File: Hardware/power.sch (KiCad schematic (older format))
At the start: 21 parts, among them IC201 FT232RQ, P201 USB_OTG, P202 CONN_01X02, U201 MCP1700T-3302E/TT

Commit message: initial footprint assignments
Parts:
- C201: renamed from C205; footprint (none) -> Capacitors_SMD:C_0805
- C202: renamed from C201; footprint (none) -> Capacitors_SMD:C_1206
- C203: renamed from C202; footprint (none) -> Capacitors_SMD:C_0805
- C204: renamed from C206; footprint (none) -> Capacitors_SMD:C_0805
- C205: renamed from C203; footprint (none) -> Capacitors_SMD:C_0805
- C206: renamed from C204; footprint (none) -> Capacitors_SMD:C_0805
- D201, D202: footprint (none) -> Diodes_SMD:D_0805
- D203, D204: footprint (none) -> LEDs:LED_0805
- IC201: footprint QFN-32 -> Housings_DFN_QFN:QFN-32-1EP_5x5mm_Pitch0.5mm
- P202: footprint (none) -> Pin_Headers:Pin_Header_Straight_1x02
- R201, R202, R203, R204, R205, R206: footprint (none) -> Resistors_SMD:R_0805
- U201: footprint (none) -> TO_SOT_Packages_SMD:SOT-23
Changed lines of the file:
@@
 F 0 "U201" H 6955 1380 50  0000 C CNN
 F 1 "MCP1700T-3302E/TT" H 6855 1880 50  0000 C CNN
-F 2 "" H 6855 1680 50  0000 C CNN
+F 2 "TO_SOT_Packages_SMD:SOT-23" H 6855 1680 50  0001 C CNN
 F 3 "http://ww1.microchip.com/downloads/en/DeviceDoc/20001826C.pdf" H 6855 1680 50  0001 C CNN
 F 4 "Value" H 6855 1580 60  0001 C CNN "Fieldname"
@@
 F 0 "IC201" H 5790 5865 50  0000 C CNN
 F 1 "FT232RQ" H 6790 3905 50  0000 C CNN
-F 2 "QFN-32" H 6340 4615 50  0000 C CIN
+F 2 "Housings_DFN_QFN:QFN-32-1EP_5x5mm_Pitch0.5mm" H 6340 4615 50  0000 C CIN
 F 3 "http://www.ftdichip.com/Support/Documents/DataSheets/ICs/DS_FT232R.pdf" H 6340 4615 50  0001 C CNN
 F 4 "Value" H 6340 4615 60  0001 C CNN "Fieldname"
@@
 Regulator Power Filtering Requirements:  1uF on input and output
 $Comp
-L C_Small C202
+L C_Small C203
 U 1 1 58D7EC21
 P 5165 3675
-F 0 "C202" H 5175 3745 50  0000 L CNN
+F 0 "C203" H 5175 3745 50  0000 L CNN
 F 1 "0.1u" H 5175 3595 50  0000 L CNN
-F 2 "" H 5165 3675 50  0000 C CNN
+F 2 "Capacitors_SMD:C_0805" H 5165 3675 50  0001 C CNN
 F 3 "" H 5165 3675 50  0000 C CNN
 F 4 "Value" H 5165 3675 60  0001 C CNN "Fieldname"
@@
 $EndComp
 $Comp
-L C_Small C201
+L C_Small C202
 U 1 1 58D7EC71
 P 4950 3675
-F 0 "C201" H 4960 3745 50  0000 L CNN
+F 0 "C202" H 4960 3745 50  0000 L CNN
 F 1 "4.7u" H 4960 3595 50  0000 L CNN
-F 2 "" H 4950 3675 50  0000 C CNN
+F 2 "Capacitors_SMD:C_1206" H 4950 3675 50  0001 C CNN
 F 3 "" H 4950 3675 50  0000 C CNN
 F 4 "Value" H 4950 3675 60  0001 C CNN "Fieldname"
@@
 $EndComp
 $Comp
-L GND #PWR204
+L GND #PWR010
 U 1 1 58D7ECC1
 P 5075 3870
-F 0 "#PWR204" H 5075 3620 50  0001 C CNN
+F 0 "#PWR010" H 5075 3620 50  0001 C CNN
 F 1 "GND" H 5075 3720 50  0000 C CNN
 F 2 "" H 5075 3870 50  0000 C CNN
@@
 $EndComp
 $Comp
-L C_Small C203
+L C_Small C205
 U 1 1 58D7EDD8
 P 6360 1580
-F 0 "C203" H 6370 1650 50  0000 L CNN
+F 0 "C205" H 6370 1650 50  0000 L CNN
 F 1 "0.1u" H 6370 1500 50  0000 L CNN
-F 2 "" H 6360 1580 50  0000 C CNN
+F 2 "Capacitors_SMD:C_0805" H 6360 1580 50  0001 C CNN
 F 3 "" H 6360 1580 50  0000 C CNN
 F 4 "Value" H 6360 1580 60  0001 C CNN "Fieldname"
@@
 $EndComp
 $Comp
-L GND #PWR207
+L GND #PWR011
 U 1 1 58D7EF23
 P 6360 1750
-F 0 "#PWR207" H 6360 1500 50  0001 C CNN
+F 0 "#PWR011" H 6360 1500 50  0001 C CNN
 F 1 "GND" H 6360 1600 50  0000 C CNN
 F 2 "" H 6360 1750 50  0000 C CNN
@@
 FTDI 3V3 Pin needs 0.1uF cap
 $Comp
-L C_Small C204
+L C_Small C206
 U 1 1 58D7F457
 P 7310 1580
-F 0 "C204" H 7320 1650 50  0000 L CNN
+F 0 "C206" H 7320 1650 50  0000 L CNN
 F 1 "0.1u" H 7320 1500 50  0000 L CNN
-F 2 "" H 7310 1580 50  0000 C CNN
+F 2 "Capacitors_SMD:C_0805" H 7310 1580 50  0001 C CNN
 F 3 "" H 7310 1580 50  0000 C CNN
 F 4 "Value" H 7310 1580 60  0001 C CNN "Fieldname"
@@
 $EndComp
 $Comp
-L GND #PWR209
+L GND #PWR012
 U 1 1 58D7F45E
 P 7310 1750
-F 0 "#PWR209" H 7310 1500 50  0001 C CNN
+F 0 "#PWR012" H 7310 1500 50  0001 C CNN
 F 1 "GND" H 7310 1600 50  0000 C CNN
 F 2 "" H 7310 1750 50  0000 C CNN
@@
 $EndComp
 $Comp
-L GND #PWR208
+L GND #PWR013
 U 1 1 58D7F4D0
 P 6855 1835
-F 0 "#PWR208" H 6855 1585 50  0001 C CNN
+F 0 "#PWR013" H 6855 1585 50  0001 C CNN
 F 1 "GND" H 6855 1685 50  0000 C CNN
 F 2 "" H 6855 1835 50  0000 C CNN
@@
 F 0 "L201" H 4710 3575 50  0000 L CNN
 F 1 "40nH" H 4710 3475 50  0000 L CNN
-F 2 "" V 4565 3525 50  0000 C CNN
+F 2 "" V 4565 3525 50  0001 C CNN
 F 3 "http://media.digikey.com/pdf/Data%20Sheets/Steward%20PDFs/Part%20Number%20Guide.pdf" H 4635 3525 50  0001 C CNN
 F 4 "Value" H 4635 3525 60  0001 C CNN "Fieldname"
@@
 $EndComp
 $Comp
-L C_Small C205
+L C_Small C201
 U 1 1 58D87D1A
 P 4345 3625
-F 0 "C205" H 4355 3695 50  0000 L CNN
+F 0 "C201" H 4355 3695 50  0000 L CNN
 F 1 "10nF" H 4355 3545 50  0000 L CNN
-F 2 "" H 4345 3625 50  0000 C CNN
+F 2 "Capacitors_SMD:C_0805" H 4345 3625 50  0001 C CNN
 F 3 "" H 4345 3625 50  0000 C CNN
 F 4 "Value" H 4345 3625 60  0001 C CNN "Fieldname"
@@
 $EndComp
 $Comp
-L GND #PWR202
+L GND #PWR014
 U 1 1 58D87E55
 P 4345 3790
-F 0 "#PWR202" H 4345 3540 50  0001 C CNN
+F 0 "#PWR014" H 4345 3540 50  0001 C CNN
 F 1 "GND" H 4345 3640 50  0000 C CNN
 F 2 "" H 4345 3790 50  0000 C CNN
@@
 F 0 "P201" H 3790 4195 50  0000 C CNN
 F 1 "USB_OTG" H 3465 4520 50  0000 C CNN
-F 2 "" V 3415 4220 50  0000 C CNN
+F 2 "" V 3415 4220 50  0001 C CNN
 F 3 "" V 3415 4220 50  0000 C CNN
 	1    3465 4320
@@
 $EndComp
 $Comp
-L GND #PWR201
+L GND #PWR015
 U 1 1 58DED01C
 P 3765 4850
-F 0 "#PWR201" H 3765 4600 50  0001 C CNN
+F 0 "#PWR015" H 3765 4600 50  0001 C CNN
 F 1 "GND" H 3765 4700 50  0000 C CNN
 F 2 "" H 3765 4850 50  0000 C CNN
@@
 F 0 "P202" H 4640 1680 50  0000 C CNN
 F 1 "CONN_01X02" V 4740 1530 50  0000 C CNN
-F 2 "" H 4640 1530 50  0000 C CNN
+F 2 "Pin_Headers:Pin_Header_Straight_1x02" H 4640 1530 50  0001 C CNN
 F 3 "" H 4640 1530 50  0000 C CNN
 	1    4640 1530
@@
 $EndComp
 $Comp
-L GND #PWR203
+L GND #PWR016
 U 1 1 58DEDB6A
 P 4840 1720
-F 0 "#PWR203" H 4840 1470 50  0001 C CNN
+F 0 "#PWR016" H 4840 1470 50  0001 C CNN
 F 1 "GND" H 4840 1570 50  0000 C CNN
 F 2 "" H 4840 1720 50  0000 C CNN
@@
 F 0 "D201" H 5015 1560 50  0000 L CNN
 F 1 "D_Schottky_Small" H 4785 1400 50  0000 L CNN
-F 2 "" V 5065 1480 50  0000 C CNN
+F 2 "Diodes_SMD:D_0805" V 5065 1480 50  0001 C CNN
 F 3 "" V 5065 1480 50  0000 C CNN
 	1    5065 1480
@@
 F 0 "D202" H 5390 2250 50  0000 L CNN
 F 1 "D_Schottky_Small" H 5160 2090 50  0000 L CNN
-F 2 "" V 5440 2170 50  0000 C CNN
+F 2 "Diodes_SMD:D_0805" V 5440 2170 50  0001 C CNN
 F 3 "" V 5440 2170 50  0000 C CNN
 	1    5440 2170
@@
 $EndComp
 $Comp
-L C_Small C206
+L C_Small C204
 U 1 1 58DEE911
 P 5275 5195
-F 0 "C206" H 5285 5265 50  0000 L CNN
+F 0 "C204" H 5285 5265 50  0000 L CNN
 F 1 "0.1u" H 5285 5115 50  0000 L CNN
-F 2 "" H 5275 5195 50  0000 C CNN
+F 2 "Capacitors_SMD:C_0805" H 5275 5195 50  0001 C CNN
 F 3 "" H 5275 5195 50  0000 C CNN
 F 4 "Value" H 5275 5195 60  0001 C CNN "Fieldname"
@@
 $EndComp
 $Comp
-L GND #PWR205
+L GND #PWR017
 U 1 1 58DEEABF
 P 5275 5345
-F 0 "#PWR205" H 5275 5095 50  0001 C CNN
+F 0 "#PWR017" H 5275 5095 50  0001 C CNN
 F 1 "GND" H 5275 5195 50  0000 C CNN
 F 2 "" H 5275 5345 50  0000 C CNN
@@
 F 0 "R201" V 7235 3470 50  0000 L CNN
 F 1 "0" V 7295 3480 50  0000 L CNN
-F 2 "" H 7295 3505 50  0000 C CNN
+F 2 "Resistors_SMD:R_0805" H 7295 3505 50  0001 C CNN
 F 3 "" H 7295 3505 50  0000 C CNN
 F 4 "Value" H 7295 3505 60  0001 C CNN "Fieldname"
@@
 F 0 "R202" V 7240 3575 50  0000 L CNN
 F 1 "0" V 7295 3590 50  0000 L CNN
-F 2 "" H 7295 3615 50  0000 C CNN
+F 2 "Resistors_SMD:R_0805" H 7295 3615 50  0001 C CNN
 F 3 "" H 7295 3615 50  0000 C CNN
 F 4 "Value" H 7295 3615 60  0001 C CNN "Fieldname"
@@
 F 0 "R203" V 7240 3715 50  0000 L CNN
 F 1 "NOPOP" V 7250 3825 50  0000 L CNN
-F 2 "" H 7295 3755 50  0000 C CNN
+F 2 "Resistors_SMD:R_0805" H 7295 3755 50  0001 C CNN
 F 3 "" H 7295 3755 50  0000 C CNN
 F 4 "Value" H 7295 3755 60  0001 C CNN "Fieldname"
@@
 F 0 "R204" V 7240 3845 50  0000 L CNN
 F 1 "NOPOP" V 7365 3810 50  0000 L CNN
-F 2 "" H 7295 3885 50  0000 C CNN
+F 2 "Resistors_SMD:R_0805" H 7295 3885 50  0001 C CNN
 F 3 "" H 7295 3885 50  0000 C CNN
 F 4 "Value" H 7295 3885 60  0001 C CNN "Fieldname"
@@
 $EndComp
 $Comp
-L GND #PWR210
+L GND #PWR018
 U 1 1 58DEFDF2
 P 7615 3885
-F 0 "#PWR210" H 7615 3635 50  0001 C CNN
+F 0 "#PWR018" H 7615 3635 50  0001 C CNN
 F 1 "GND" H 7615 3735 50  0000 C CNN
 F 2 "" H 7615 3885 50  0000 C CNN
@@
 F 0 "D203" H 7890 4360 50  0000 C CNN
 F 1 "GRN LED" H 7890 4160 50  0000 C CNN
-F 2 "" H 7890 4260 50  0000 C CNN
+F 2 "LEDs:LED_0805" H 7890 4260 50  0001 C CNN
 F 3 "" H 7890 4260 50  0000 C CNN
 F 4 "Value" H 7890 4260 60  0001 C CNN "Fieldname"
@@
 F 0 "D204" H 8200 4365 50  0000 C CNN
 F 1 "YLW LED" H 8200 4165 50  0000 C CNN
-F 2 "" H 8200 4265 50  0000 C CNN
+F 2 "LEDs:LED_0805" H 8200 4265 50  0001 C CNN
 F 3 "" H 8200 4265 50  0000 C CNN
 	1    8200 4265
@@
 F 0 "R205" V 7835 3915 50  0000 L CNN
 F 1 "330" V 7965 3890 50  0000 L CNN
-F 2 "" H 7890 3955 50  0000 C CNN
+F 2 "Resistors_SMD:R_0805" H 7890 3955 50  0001 C CNN
 F 3 "" H 7890 3955 50  0000 C CNN
 F 4 "Value" H 7890 3955 60  0001 C CNN "Fieldname"
@@
 F 0 "R206" V 8145 3915 50  0000 L CNN
 F 1 "330" V 8270 3890 50  0000 L CNN
-F 2 "" H 8200 3955 50  0000 C CNN
+F 2 "Resistors_SMD:R_0805" H 8200 3955 50  0001 C CNN
 F 3 "" H 8200 3955 50  0000 C CNN
 F 4 "Value" H 8200 3955 60  0001 C CNN "Fieldname"
@@
 NoConn ~ 7090 4045
 $Comp
-L GND #PWR206
+L GND #PWR019
 U 1 1 58DF3EAD
 P 6315 5730
-F 0 "#PWR206" H 6315 5480 50  0001 C CNN
+F 0 "#PWR019" H 6315 5480 50  0001 C CNN
 F 1 "GND" H 6315 5580 50  0000 C CNN
 F 2 "" H 6315 5730 50  0000 C CNN

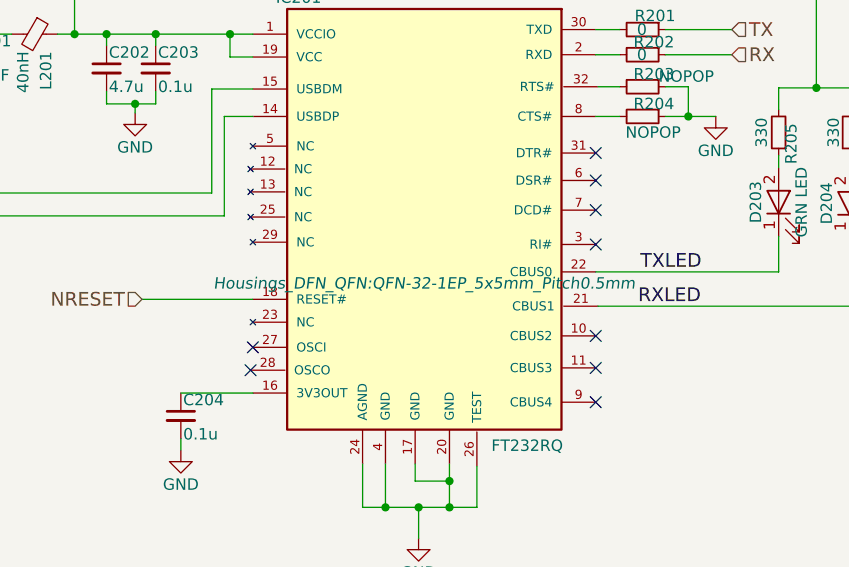
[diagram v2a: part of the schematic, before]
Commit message: added crystal details and usb footprint
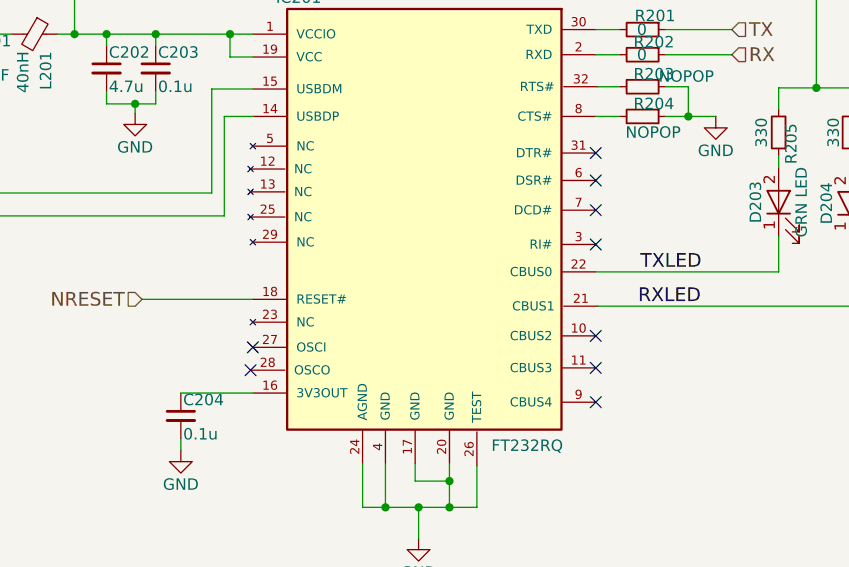
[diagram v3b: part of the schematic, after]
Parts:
- L201: footprint (none) -> Capacitors_SMD:C_0805
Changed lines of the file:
@@
 F 0 "IC201" H 5790 5865 50  0000 C CNN
 F 1 "FT232RQ" H 6790 3905 50  0000 C CNN
-F 2 "Housings_DFN_QFN:QFN-32-1EP_5x5mm_Pitch0.5mm" H 6340 4615 50  0000 C CIN
+F 2 "Housings_DFN_QFN:QFN-32-1EP_5x5mm_Pitch0.5mm" H 6340 4615 50  0001 C CIN
 F 3 "http://www.ftdichip.com/Support/Documents/DataSheets/ICs/DS_FT232R.pdf" H 6340 4615 50  0001 C CNN
 F 4 "Value" H 6340 4615 60  0001 C CNN "Fieldname"
@@
 $EndComp
 $Comp
-L GND #PWR010
+L GND #PWR012
 U 1 1 58D7ECC1
 P 5075 3870
-F 0 "#PWR010" H 5075 3620 50  0001 C CNN
+F 0 "#PWR012" H 5075 3620 50  0001 C CNN
 F 1 "GND" H 5075 3720 50  0000 C CNN
 F 2 "" H 5075 3870 50  0000 C CNN
@@
 $EndComp
 $Comp
-L GND #PWR011
+L GND #PWR013
 U 1 1 58D7EF23
 P 6360 1750
-F 0 "#PWR011" H 6360 1500 50  0001 C CNN
+F 0 "#PWR013" H 6360 1500 50  0001 C CNN
 F 1 "GND" H 6360 1600 50  0000 C CNN
 F 2 "" H 6360 1750 50  0000 C CNN
@@
 $EndComp
 $Comp
-L GND #PWR012
+L GND #PWR014
 U 1 1 58D7F45E
 P 7310 1750
-F 0 "#PWR012" H 7310 1500 50  0001 C CNN
+F 0 "#PWR014" H 7310 1500 50  0001 C CNN
 F 1 "GND" H 7310 1600 50  0000 C CNN
 F 2 "" H 7310 1750 50  0000 C CNN
@@
 $EndComp
 $Comp
-L GND #PWR013
+L GND #PWR015
 U 1 1 58D7F4D0
 P 6855 1835
-F 0 "#PWR013" H 6855 1585 50  0001 C CNN
+F 0 "#PWR015" H 6855 1585 50  0001 C CNN
 F 1 "GND" H 6855 1685 50  0000 C CNN
 F 2 "" H 6855 1835 50  0000 C CNN
@@
 F 0 "L201" H 4710 3575 50  0000 L CNN
 F 1 "40nH" H 4710 3475 50  0000 L CNN
-F 2 "" V 4565 3525 50  0001 C CNN
+F 2 "Capacitors_SMD:C_0805" V 4565 3525 50  0001 C CNN
 F 3 "http://media.digikey.com/pdf/Data%20Sheets/Steward%20PDFs/Part%20Number%20Guide.pdf" H 4635 3525 50  0001 C CNN
 F 4 "Value" H 4635 3525 60  0001 C CNN "Fieldname"
@@
 $EndComp
 $Comp
-L GND #PWR014
+L GND #PWR016
 U 1 1 58D87E55
 P 4345 3790
-F 0 "#PWR014" H 4345 3540 50  0001 C CNN
+F 0 "#PWR016" H 4345 3540 50  0001 C CNN
 F 1 "GND" H 4345 3640 50  0000 C CNN
 F 2 "" H 4345 3790 50  0000 C CNN
@@
 $EndComp
 $Comp
-L GND #PWR015
+L GND #PWR017
 U 1 1 58DED01C
 P 3765 4850
-F 0 "#PWR015" H 3765 4600 50  0001 C CNN
+F 0 "#PWR017" H 3765 4600 50  0001 C CNN
 F 1 "GND" H 3765 4700 50  0000 C CNN
 F 2 "" H 3765 4850 50  0000 C CNN
@@
 $EndComp
 $Comp
-L GND #PWR016
+L GND #PWR018
 U 1 1 58DEDB6A
 P 4840 1720
-F 0 "#PWR016" H 4840 1470 50  0001 C CNN
+F 0 "#PWR018" H 4840 1470 50  0001 C CNN
 F 1 "GND" H 4840 1570 50  0000 C CNN
 F 2 "" H 4840 1720 50  0000 C CNN
@@
 $EndComp
 $Comp
-L GND #PWR017
+L GND #PWR019
 U 1 1 58DEEABF
 P 5275 5345
-F 0 "#PWR017" H 5275 5095 50  0001 C CNN
+F 0 "#PWR019" H 5275 5095 50  0001 C CNN
 F 1 "GND" H 5275 5195 50  0000 C CNN
 F 2 "" H 5275 5345 50  0000 C CNN
@@
 $EndComp
 $Comp
-L GND #PWR018
+L GND #PWR020
 U 1 1 58DEFDF2
 P 7615 3885
-F 0 "#PWR018" H 7615 3635 50  0001 C CNN
+F 0 "#PWR020" H 7615 3635 50  0001 C CNN
 F 1 "GND" H 7615 3735 50  0000 C CNN
 F 2 "" H 7615 3885 50  0000 C CNN
@@
 NoConn ~ 7090 4045
 $Comp
-L GND #PWR019
+L GND #PWR021
 U 1 1 58DF3EAD
 P 6315 5730
-F 0 "#PWR019" H 6315 5480 50  0001 C CNN
+F 0 "#PWR021" H 6315 5480 50  0001 C CNN
 F 1 "GND" H 6315 5580 50  0000 C CNN
 F 2 "" H 6315 5730 50  0000 C CNN

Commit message: changed grove connectors to jst sh and added VCC and GND to other headers
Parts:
- P201: footprint (none) -> CentralCommand:10118193; Fieldname (none) -> Value; MPN (none) -> 10118193-0001LF
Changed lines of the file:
@@
 $EndComp
 $Comp
-L GND #PWR012
+L GND #PWR09
 U 1 1 58D7ECC1
 P 5075 3870
-F 0 "#PWR012" H 5075 3620 50  0001 C CNN
+F 0 "#PWR09" H 5075 3620 50  0001 C CNN
 F 1 "GND" H 5075 3720 50  0000 C CNN
 F 2 "" H 5075 3870 50  0000 C CNN
@@
 $EndComp
 $Comp
-L GND #PWR013
+L GND #PWR010
 U 1 1 58D7EF23
 P 6360 1750
-F 0 "#PWR013" H 6360 1500 50  0001 C CNN
+F 0 "#PWR010" H 6360 1500 50  0001 C CNN
 F 1 "GND" H 6360 1600 50  0000 C CNN
 F 2 "" H 6360 1750 50  0000 C CNN
@@
 $EndComp
 $Comp
-L GND #PWR014
+L GND #PWR011
 U 1 1 58D7F45E
 P 7310 1750
-F 0 "#PWR014" H 7310 1500 50  0001 C CNN
+F 0 "#PWR011" H 7310 1500 50  0001 C CNN
 F 1 "GND" H 7310 1600 50  0000 C CNN
 F 2 "" H 7310 1750 50  0000 C CNN
@@
 $EndComp
 $Comp
-L GND #PWR015
+L GND #PWR012
 U 1 1 58D7F4D0
 P 6855 1835
-F 0 "#PWR015" H 6855 1585 50  0001 C CNN
+F 0 "#PWR012" H 6855 1585 50  0001 C CNN
 F 1 "GND" H 6855 1685 50  0000 C CNN
 F 2 "" H 6855 1835 50  0000 C CNN
@@
 $EndComp
 $Comp
-L GND #PWR016
+L GND #PWR013
 U 1 1 58D87E55
 P 4345 3790
-F 0 "#PWR016" H 4345 3540 50  0001 C CNN
+F 0 "#PWR013" H 4345 3540 50  0001 C CNN
 F 1 "GND" H 4345 3640 50  0000 C CNN
 F 2 "" H 4345 3790 50  0000 C CNN
@@
 F 0 "P201" H 3790 4195 50  0000 C CNN
 F 1 "USB_OTG" H 3465 4520 50  0000 C CNN
-F 2 "" V 3415 4220 50  0001 C CNN
-F 3 "" V 3415 4220 50  0000 C CNN
+F 2 "CentralCommand:10118193" V 3415 4220 50  0001 C CNN
+F 3 "http://portal.fciconnect.com/Comergent//fci/drawing/10118193.pdf" V 3415 4220 50  0001 C CNN
+F 4 "Value" H 3465 4320 60  0001 C CNN "Fieldname"
+F 5 "10118193-0001LF" H 3465 4320 60  0001 C CNN "MPN"
 	1    3465 4320
 	0    -1   1    0
 $EndComp
 $Comp
-L GND #PWR017
+L GND #PWR014
 U 1 1 58DED01C
 P 3765 4850
-F 0 "#PWR017" H 3765 4600 50  0001 C CNN
+F 0 "#PWR014" H 3765 4600 50  0001 C CNN
 F 1 "GND" H 3765 4700 50  0000 C CNN
 F 2 "" H 3765 4850 50  0000 C CNN
@@
 $EndComp
 $Comp
-L GND #PWR018
+L GND #PWR015
 U 1 1 58DEDB6A
 P 4840 1720
-F 0 "#PWR018" H 4840 1470 50  0001 C CNN
+F 0 "#PWR015" H 4840 1470 50  0001 C CNN
 F 1 "GND" H 4840 1570 50  0000 C CNN
 F 2 "" H 4840 1720 50  0000 C CNN
@@
 $EndComp
 $Comp
-L GND #PWR019
+L GND #PWR016
 U 1 1 58DEEABF
 P 5275 5345
-F 0 "#PWR019" H 5275 5095 50  0001 C CNN
+F 0 "#PWR016" H 5275 5095 50  0001 C CNN
 F 1 "GND" H 5275 5195 50  0000 C CNN
 F 2 "" H 5275 5345 50  0000 C CNN
@@
 $EndComp
 $Comp
-L GND #PWR020
+L GND #PWR017
 U 1 1 58DEFDF2
 P 7615 3885
-F 0 "#PWR020" H 7615 3635 50  0001 C CNN
+F 0 "#PWR017" H 7615 3635 50  0001 C CNN
 F 1 "GND" H 7615 3735 50  0000 C CNN
 F 2 "" H 7615 3885 50  0000 C CNN
@@
 NoConn ~ 7090 4045
 $Comp
-L GND #PWR021
+L GND #PWR018
 U 1 1 58DF3EAD
 P 6315 5730
-F 0 "#PWR021" H 6315 5480 50  0001 C CNN
+F 0 "#PWR018" H 6315 5480 50  0001 C CNN
 F 1 "GND" H 6315 5580 50  0000 C CNN
 F 2 "" H 6315 5730 50  0000 C CNN
